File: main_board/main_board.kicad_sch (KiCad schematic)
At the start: 8 parts, among them U2 TS5A4624DCKR, U4 TS5A4624DCKR

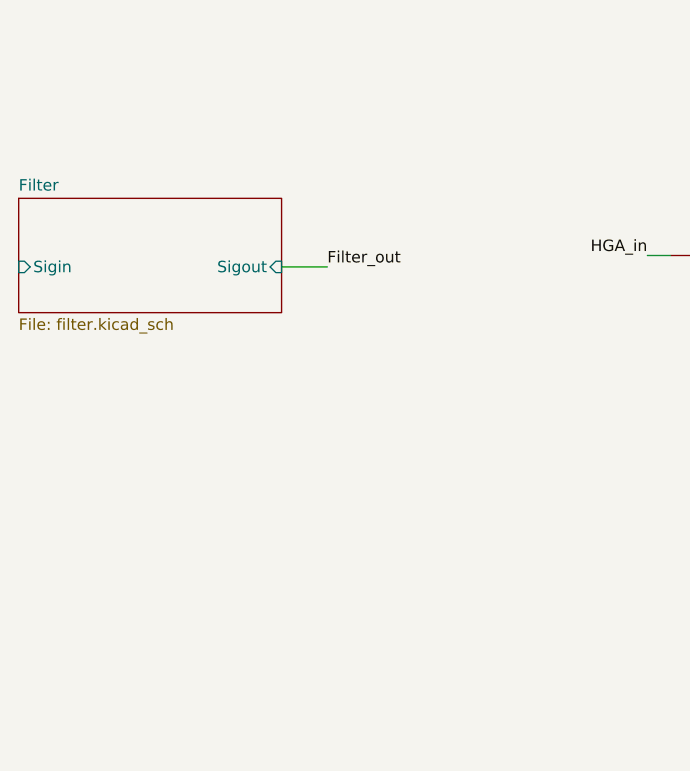
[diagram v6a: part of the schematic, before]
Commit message: add IO description textbox
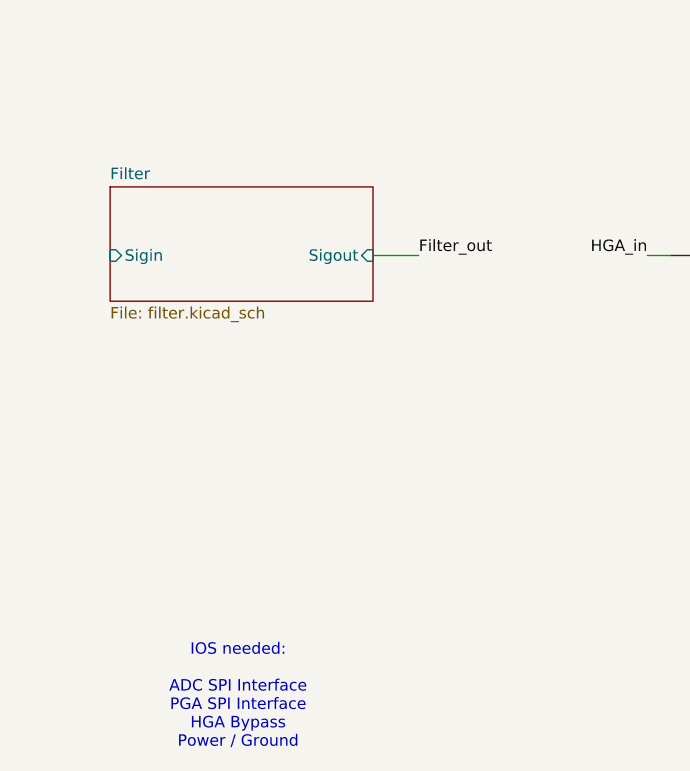
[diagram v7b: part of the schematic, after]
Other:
- note added: "IOS needed: ADC SPI Interface PGA SPI Interface HGA Bypass Power / Ground"
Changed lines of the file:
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@@
+		)
+	)
+	(text "IOS needed: \n\nADC SPI Interface\nPGA SPI Interface \nHGA Bypass \nPower / Ground"
+		(exclude_from_sim no)
+		(at 44.704 129.032 0)
+		(effects
+			(font
+				(size 1.27 1.27)
+			)
 		)
 	)
@@
 	(wire
 		(pts
-			(xy 49.53 81.28) (xy 54.61 81.28)
+			(xy 59.69 80.01) (xy 64.77 80.01)
 		)
 		(stroke
@@
 	)
 	(label "Filter_out"
-		(at 54.61 81.28 0)
+		(at 64.77 80.01 0)
 		(effects
 			(font
@@
 	)
 	(sheet
-		(at 20.32 73.66)
+		(at 30.48 72.39)
 		(size 29.21 12.7)
 		(exclude_from_sim no)
@@
 		)
 		(property "Sheetname" "Filter"
-			(at 20.32 72.9484 0)
+			(at 30.48 71.6784 0)
 			(effects
 				(font
@@
 		)
 		(property "Sheetfile" "filter.kicad_sch"
-			(at 20.32 86.9446 0)
+			(at 30.48 85.6746 0)
 			(effects
 				(font
@@
 		)
 		(pin "Sigin" input
-			(at 20.32 81.28 180)
+			(at 30.48 80.01 180)
 			(effects
 				(font
@@
 		)
 		(pin "Sigout" input
-			(at 49.53 81.28 0)
-			(effects
-				(font
+			(at 59.69 80.01 0)
+			(effects
+				(font

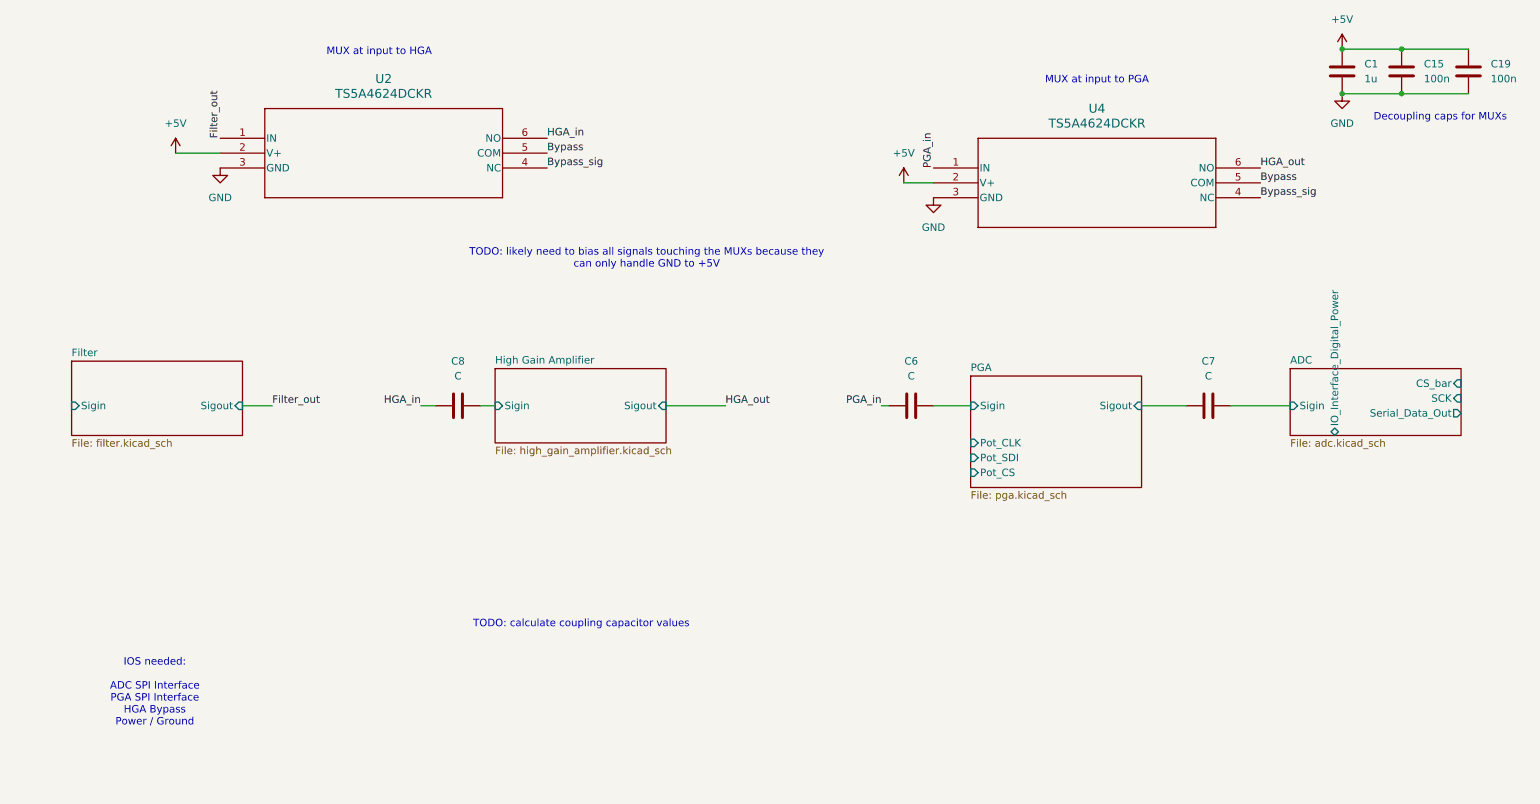
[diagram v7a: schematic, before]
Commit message: add biasing before first mux, update IO comment
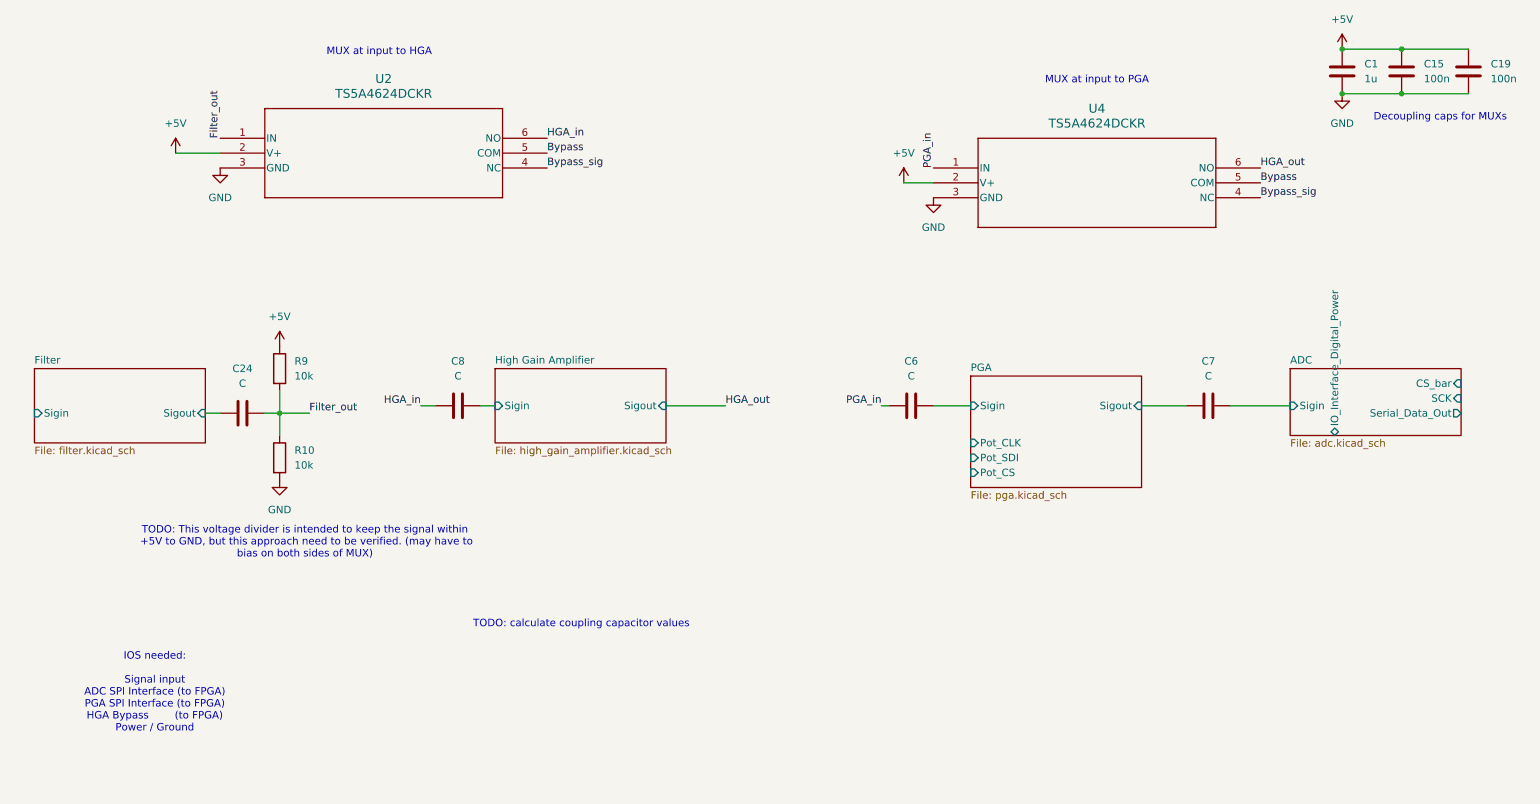
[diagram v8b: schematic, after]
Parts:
- added C24: C, symbol Device:C
- added R10, R9: 10k, symbol Device:R
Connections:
- net +5V: now also R9.1
- net Filter_out: now also C24.2, R10.1, R9.2
- net GND: now also R10.2
- new net Filter/Sigout: C24.1
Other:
- note added: "IOS needed: Signal input ADC SPI Interface (to FPGA) PGA SPI Interface (to FPGA) HGA Bypass (to FPGA) Power / Ground"
- note added: "TODO: This voltage divider is intended to keep the signal within +5V to GND, but this approach need to be verified. (may have to bias on both sides of MUX)"
- note removed: "IOS needed: ADC SPI Interface PGA SPI Interface HGA Bypass Power / Ground"
- note removed: "TODO: likely need to bias all signals touching the MUXs because they can only handle GND to +5V"
